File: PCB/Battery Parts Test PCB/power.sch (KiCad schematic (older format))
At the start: 1 part

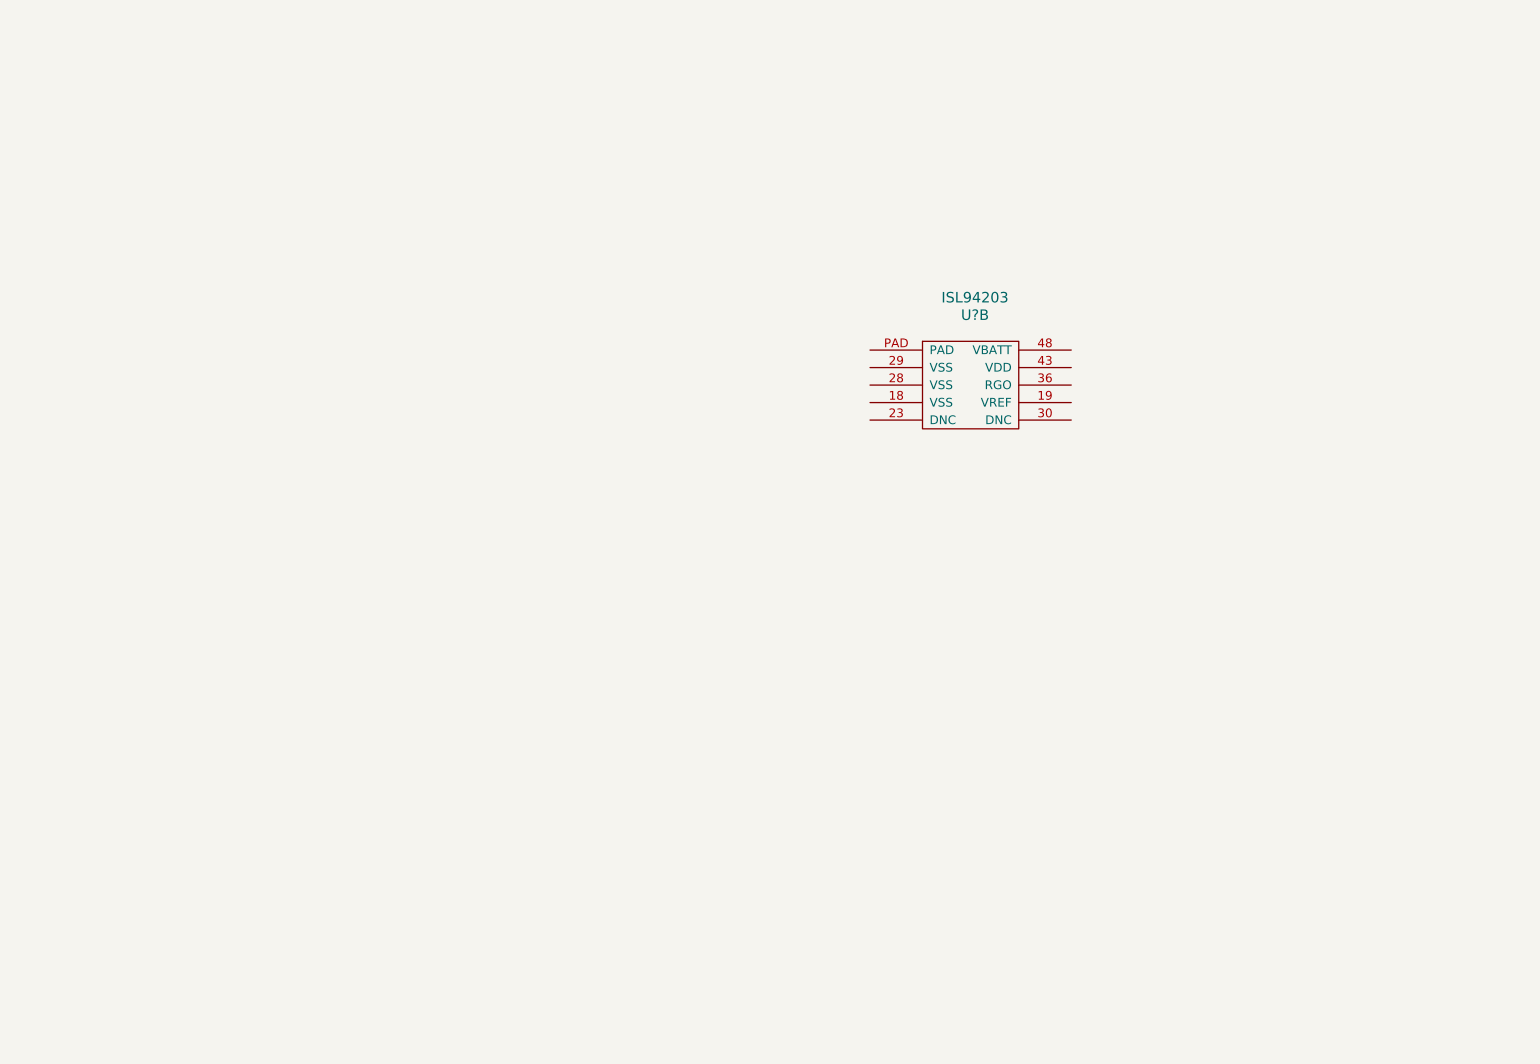
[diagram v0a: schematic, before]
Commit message: first draft schematic complete for bat mon
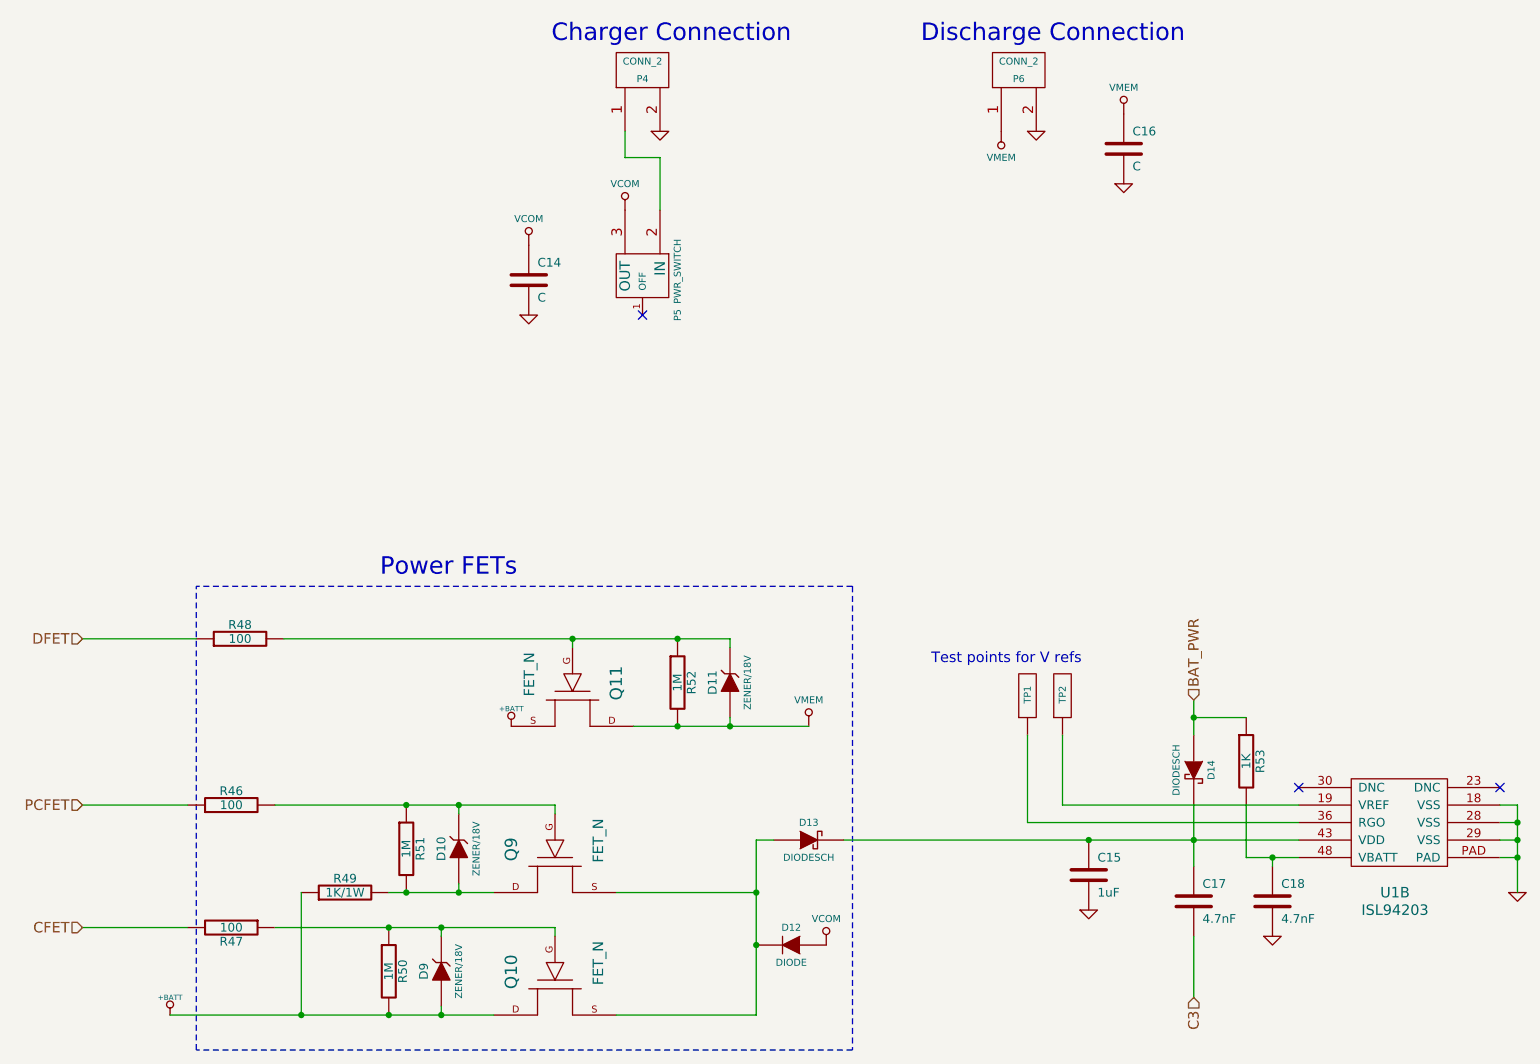
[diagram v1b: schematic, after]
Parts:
- added C14, C16: C, symbol C
- added C15: 1uF, symbol C
- added C17, C18: 4.7nF, symbol C
- added D10, D11, D9: ZENER/18V, symbol ZENER
- added D12: DIODE, symbol DIODE
- added D13, D14: DIODESCH, symbol DIODESCH
- added P4, P6: CONN_2, symbol CONN_2
- added P5: PWR_SWITCH, symbol PWR_SWITCH
- added Q10, Q11, Q9: FET_N, symbol FET_N
- added R46, R47, R48: 100, symbol R
- added R49: 1K/1W, symbol R
- added R50, R51, R52: 1M, symbol R
- added R53: 1K, symbol R
- added TP1, TP2: TEST_POINT, symbol TEST_POINT
- gave numbers to parts that had none: 1
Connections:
- net GND: now reaches U1.18 (VSS)
- net GND: now also U1.28 (VSS), U1.29 (VSS), U1.PAD, C14.2, C15.2, C16.2, C18.2, P4.2 (PM), P6.2 (PM)
- net at U1.19 (VREF): now also TP2.1
- net at U1.36 (RGO): now also TP1.1
- net at U1.43 (VDD): now also C15.1, C17.1, D13.2 (K), D14.2 (K)
- net at U1.48 (VBATT): now also C18.1, R53.2
- new net: P4.1 (P1), P5.2 (IN)
- new net: D10.1 (A), Q9.D, R49.2, R51.2
- new net: D12.2 (K), D13.1 (A), Q10.S, Q9.S
- new net: D11.2 (K), Q11.G, R48.2, R52.1
- new net: D10.2 (K), Q9.G, R46.2, R51.1
- new net: D9.2 (K), Q10.G, R47.1, R50.1
- new net +BATT: D9.1 (A), Q10.D, Q11.S, R49.1, R50.2
- new net BAT_PWR: D14.1 (A), R53.1
- new net C3: C17.2
- new net CFET: R47.2
- new net DFET: R48.1
- new net PCFET: R46.1
- new net VCOM: C14.1, D12.1 (A), P5.3 (OUT)
- new net VMEM: C16.1, D11.1 (A), P6.1 (P1), Q11.D, R52.2
- no-connect marks 0 -> 3
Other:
- note added: "Charger Connection"
- note added: "Discharge Connection"
- note added: "Power FETs"
- note added: "Test points for V refs"
- moved on the sheet: U1B
